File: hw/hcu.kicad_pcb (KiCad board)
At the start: 2 copper layers, 78 x 90 mm, 119 parts, among them J101 AMPSEAL_23_POS_VERT_BLACK_SEA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, J102 AMPSEAL_8_POS_VERT_BLACK_SEAL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, J201 ARM_JTAG_SWD_HEADER_10_PINSMD, U1001 VND5050AJTR-E, U1101 VND5050AJTR-E, U1201 VND5050AJTR-E, U1401 VN5E010AH, U201 MCP2551_SOIC8, U202 LPC1549JBD64, U301 VND5050AJTR-E, U401 VND5050AJTR-E, U501 VND5050AJTR-E, U601 VND5050AJTR-E, U701 VND5050AJTR-E, U801 VND5050AJTR-E, U901 VND5050AJTR-E, X201 XTAL_7A-12.000MAAJ-T

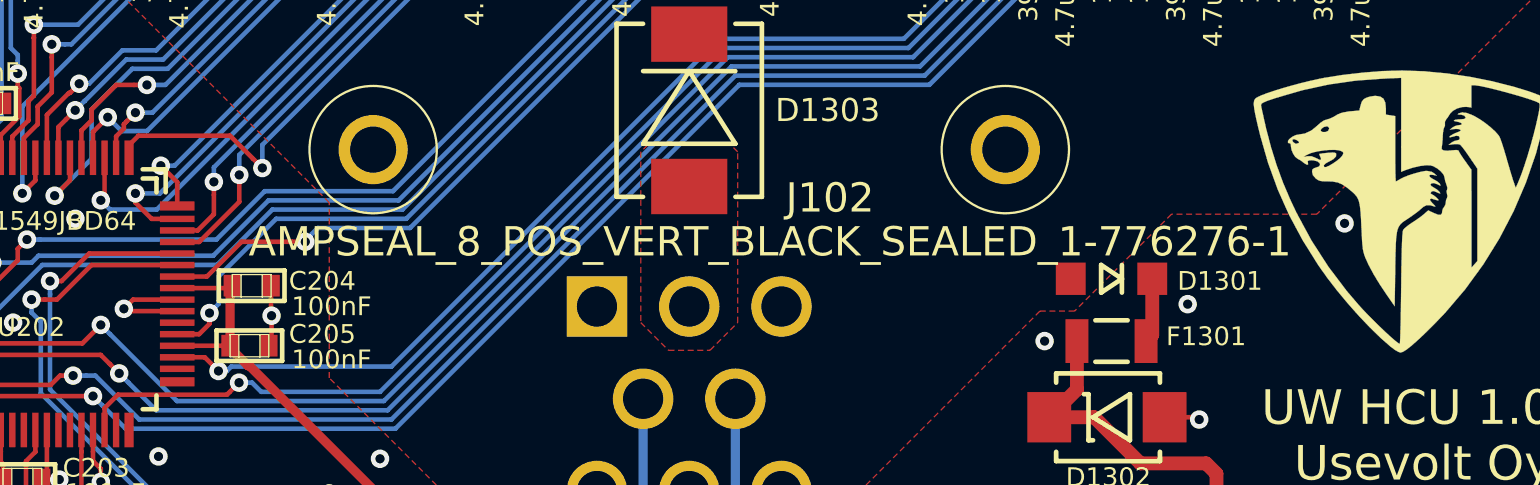
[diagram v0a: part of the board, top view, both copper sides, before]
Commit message: ampseal 8 pin changed to white one
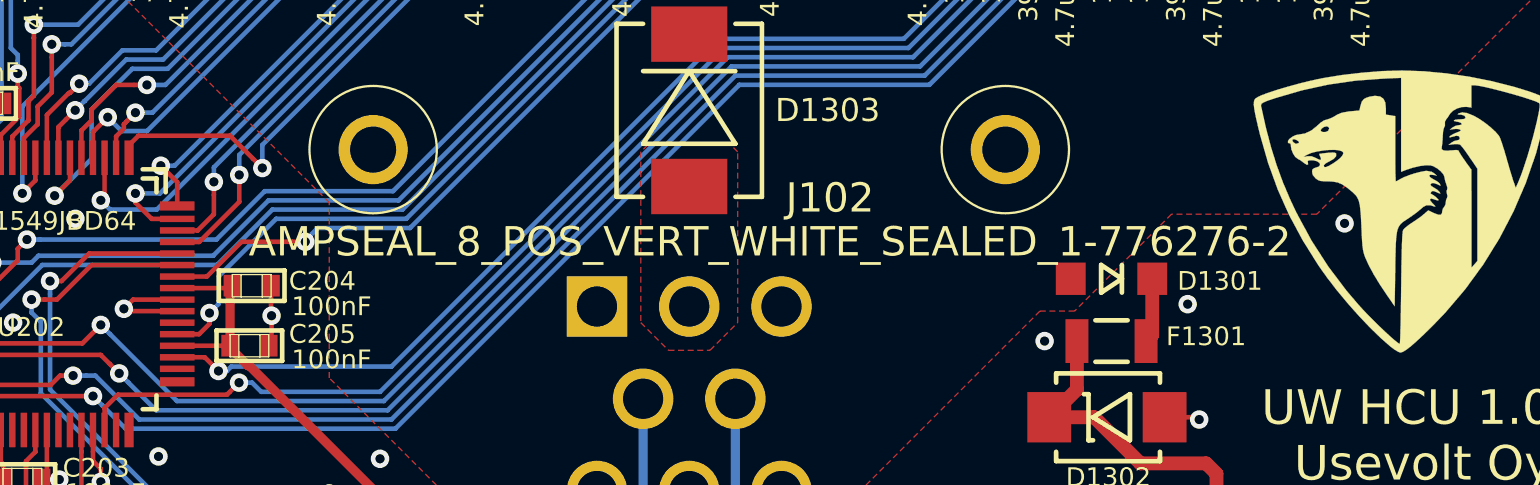
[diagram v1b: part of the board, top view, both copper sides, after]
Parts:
- J102: value AMPSEAL_8_POS_VERT_BLACK_SEALED_1-776276-1 -> AMPSEAL_8_POS_VERT_WHITE_SEALED_1-776276-2
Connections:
- J102 pad 6: VDD -> (no net)
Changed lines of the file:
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@@
     (add_net VDD)
   )
+  (module usevolt:SOT-23_3-PIN (layer F.Cu)
+    (at 160.354139 134.346 180)
+    (attr smd)
+    (fp_text reference VR1302 (at 0.354139 -2.754 180) (layer F.SilkS)
+      (effects (font (size 0.8128 0.8128) (thickness 0.0762)))
+    )
+    (fp_text value REG_MCP1700 (at 6 0 180) (layer F.SilkS) hide
+      (effects (font (size 0.8128 0.8128) (thickness 0.0762)))
+    )
+    (fp_line (start 1.4478 -0.54958) (end -1.4478 -0.54958) (layer F.SilkS) (width 0.19812))
+    (fp_line (start -1.4478 -0.54958) (end -1.4478 0.54958) (layer F.SilkS) (width 0.19812))
+    (fp_line (start 1.4478 -0.54958) (end 1.4478 0.54958) (layer F.SilkS) (width 0.19812))
+    (fp_line (start 1.4478 0.54958) (end -1.4478 0.54958) (layer F.SilkS) (width 0.19812))
+    (pad 1 smd rect (at -1 1.3 180) (size 0.7 1.35) (layers F.Cu F.Paste F.Mask)
+      (net 1 GND))
+    (pad 2 smd rect (at 1 1.3 180) (size 0.7 1.35) (layers F.Cu F.Paste F.Mask)
+      (net 2 +3V3))
+    (pad 3 smd rect (at 0 -1.3 180) (size 0.7 1.35) (layers F.Cu F.Paste F.Mask)
+      (net 3 +5V))
+    (model ${KISYS3DMOD}/SOT-23.wrl
+      (at (xyz 0 0 0))
+      (scale (xyz 0.3937 0.3937 0.3937))
+      (rotate (xyz 0 0 180))
+    )
+  )
   (module usevolt:uw_logo locked (layer F.Cu)
     (at 198.8 114.8)
@@
     )
   )
-  (module usevolt:SOT-23_3-PIN (layer F.Cu)
-    (at 160.354139 134.346 180)
-    (attr smd)
-    (fp_text reference VR1302 (at 0.354139 -2.754 180) (layer F.SilkS)
-      (effects (font (size 0.8128 0.8128) (thickness 0.0762)))
-    )
-    (fp_text value REG_MCP1700 (at 6 0 180) (layer F.SilkS) hide
-      (effects (font (size 0.8128 0.8128) (thickness 0.0762)))
-    )
-    (fp_line (start 1.4478 0.54958) (end -1.4478 0.54958) (layer F.SilkS) (width 0.19812))
-    (fp_line (start 1.4478 -0.54958) (end 1.4478 0.54958) (layer F.SilkS) (width 0.19812))
-    (fp_line (start -1.4478 -0.54958) (end -1.4478 0.54958) (layer F.SilkS) (width 0.19812))
-    (fp_line (start 1.4478 -0.54958) (end -1.4478 -0.54958) (layer F.SilkS) (width 0.19812))
-    (pad P$3 smd rect (at 0 -1.3 180) (size 0.7 1.35) (layers F.Cu F.Paste F.Mask)
-      (net 3 +5V))
-    (pad P$2 smd rect (at 1 1.3 180) (size 0.7 1.35) (layers F.Cu F.Paste F.Mask)
-      (net 2 +3V3))
-    (pad P$1 smd rect (at -1 1.3 180) (size 0.7 1.35) (layers F.Cu F.Paste F.Mask)
-      (net 1 GND))
-    (model ${KISYS3DMOD}/SOT-23.wrl
-      (at (xyz 0 0 0))
-      (scale (xyz 0.3937 0.3937 0.3937))
-      (rotate (xyz 0 0 180))
-    )
-  )
   (module usevolt:XTAL_7A-20.000MAJ (layer F.Cu)
     (at 133.8 130.4)
@@
       (effects (font (size 1.27 1.27) (thickness 0.1016)))
     )
-    (fp_text value AMPSEAL_8_POS_VERT_BLACK_SEALED_1-776276-1 (at 3.5 -6.8) (layer F.SilkS)
+    (fp_text value AMPSEAL_8_POS_VERT_WHITE_SEALED_1-776276-2 (at 3.5 -6.8) (layer F.SilkS)
       (effects (font (size 1.27 1.27) (thickness 0.1016)))
     )
@@
     (pad 5 thru_hole circle (at 1.99898 0) (size 2.62382 2.62382) (drill 1.74752) (layers *.Cu *.Mask)
       (net 9 /lpc1549/CANL))
-    (pad 6 thru_hole circle (at -3.99796 3.99796) (size 2.62382 2.62382) (drill 1.74752) (layers *.Cu *.Mask)
-      (net 4 VDD))
+    (pad 6 thru_hole circle (at -3.99796 3.99796) (size 2.62382 2.62382) (drill 1.74752) (layers *.Cu *.Mask))
     (pad 7 thru_hole circle (at 0 3.99796) (size 2.62382 2.62382) (drill 1.74752) (layers *.Cu *.Mask))
     (pad 8 thru_hole circle (at 3.99796 3.99796) (size 2.62382 2.62382) (drill 1.74752) (layers *.Cu *.Mask))

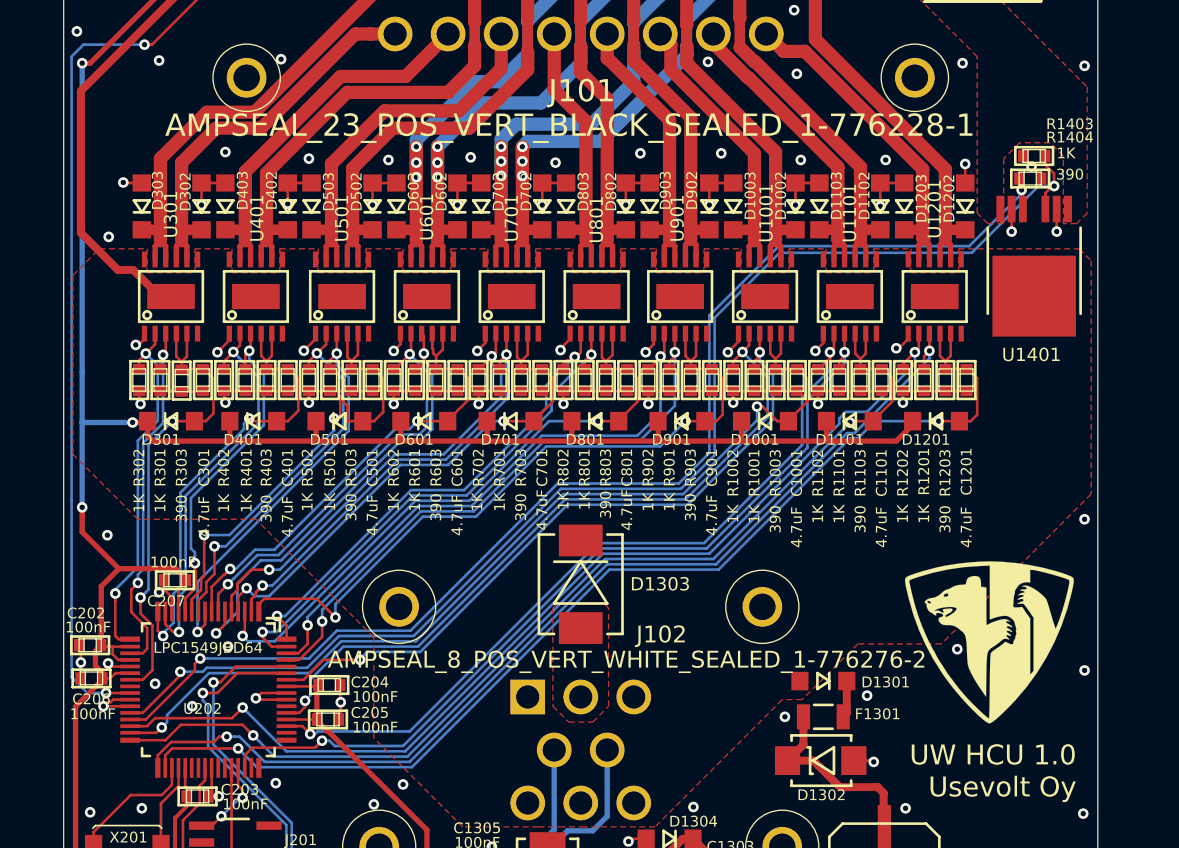
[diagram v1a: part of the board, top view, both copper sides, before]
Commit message: pull down resistor and flyback diode added to out11
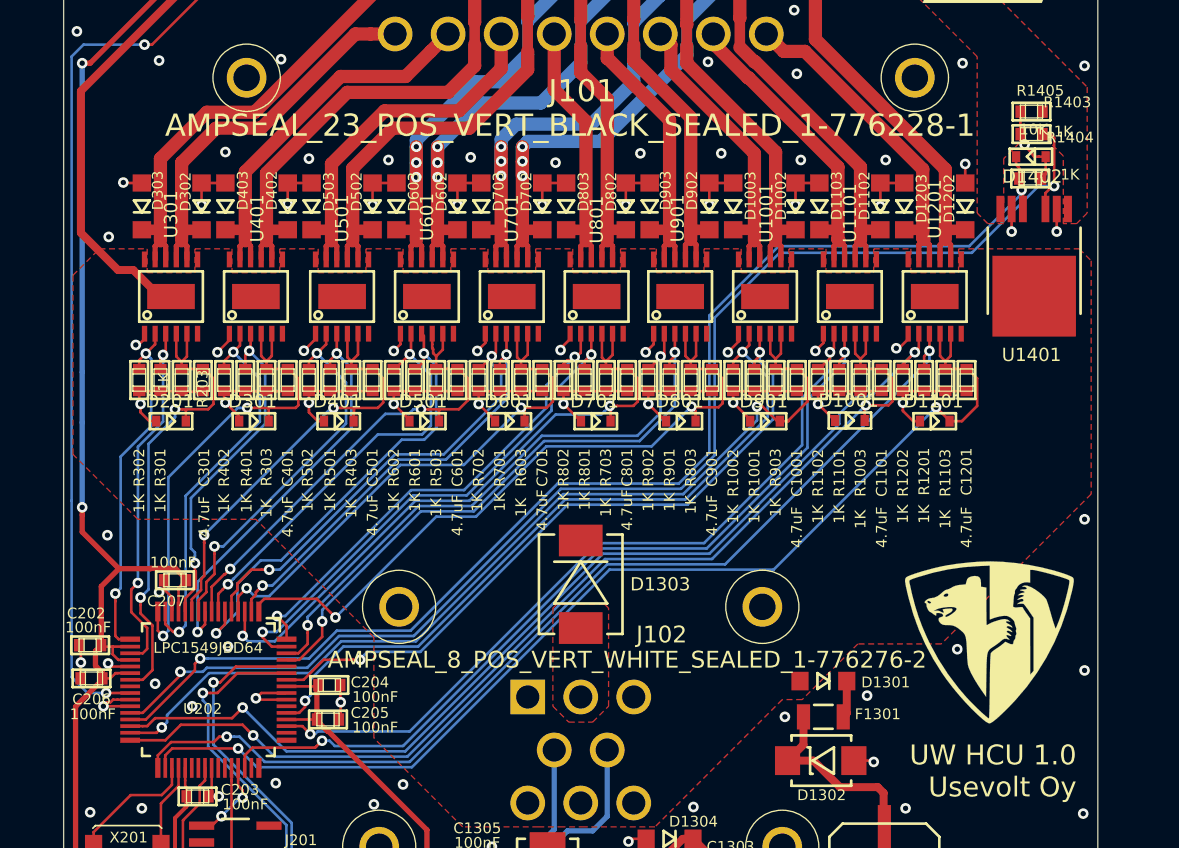
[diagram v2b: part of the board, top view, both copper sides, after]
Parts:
- removed D1201: DIODE_RS07J-GS18, usevolt:DO219AB
- removed R1203: 390, yageo:0603
- added D1402: ZENER_MM3Z3V6T1G, usevolt:SOD-323, F.Cu at (201.9, 78.2)
- added D201: ZENER_MM3Z3V6T1G, usevolt:SOD-323, F.Cu at (137.1, 98.2)
- added R1405: 10K, yageo:0603, F.Cu at (202.0, 74.8)
- added R203: 1K, yageo:0603, F.Cu at (137.9, 95.1)
- D1001, D1101, D301, D401, D501, D601, D701, D801, D901: value DIODE_RS07J-GS18 -> ZENER_MM3Z3V6T1G; footprint usevolt:DO219AB -> usevolt:SOD-323
- R1003, R1103, R1404, R303, R403, R503, R603, R703, R803, R903: value 390 -> 1K
- moved D601 6.45 mm to (162.7, 98.2)
- moved D801 6.45 mm to (175.6, 98.2)
- moved D401 6.45 mm to (149.8, 98.2)
- moved D701 6.44 mm to (169.1, 98.2)
- moved D1001 6.40 mm to (188.3, 98.2)
- moved R303 6.40 mm to (144.3, 95.1)
- moved R1003 6.40 mm to (189.1, 95.1)
- moved R1103 6.40 mm to (195.5, 95.1)
- moved R503 6.40 mm to (157.1, 95.1)
- moved R603 6.40 mm to (163.5, 95.1)
- moved R703 6.40 mm to (169.9, 95.1)
- moved R803 6.40 mm to (176.3, 95.1)
- moved D1101 6.40 mm to (194.7, 98.2)
- moved D501 6.40 mm to (156.2, 98.2)
- moved R403 6.40 mm to (150.7, 95.1)
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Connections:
- R1003 pad 1: /lpc1549/OUT8_SENSE -> /lpc1549/OUT9_SENSE
- R1103 pad 1: /lpc1549/OUT9_SENSE -> /lpc1549/OUT10_SENSE
- R303 pad 1: /lpc1549/OUT1_SENSE -> /lpc1549/OUT2_SENSE
- R403 pad 1: /lpc1549/OUT2_SENSE -> /lpc1549/OUT3_SENSE
- R503 pad 1: /lpc1549/OUT3_SENSE -> /lpc1549/OUT4_SENSE
- R603 pad 1: /lpc1549/OUT4_SENSE -> /lpc1549/OUT5_SENSE
- R703 pad 1: /lpc1549/OUT5_SENSE -> /lpc1549/OUT6_SENSE
- R803 pad 1: /lpc1549/OUT6_SENSE -> /lpc1549/OUT7_SENSE
- R903 pad 1: /lpc1549/OUT7_SENSE -> /lpc1549/OUT8_SENSE
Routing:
- net +3V3: track 266.9 -> 190.1 mm, vias 3 -> 2
- net GND: track 160.2 -> 183.8 mm
- net /lpc1549/OUT3_SENSE: track 37.6 -> 34.4 mm
- net /Sheet5ABCCFA6/IN1: track 96.9 -> 99.1 mm
- net /lpc1549/OUT11_SENSE: track 92.7 -> 94.5 mm
- net /lpc1549/OUT2_SENSE: track 35.4 -> 37.0 mm
- net /lpc1549/OUT9_SENSE: track 79.4 -> 80.6 mm
- net /lpc1549/OUT6_SENSE: track 48.9 -> 50.1 mm
- net /lpc1549/OUT5_SENSE: track 41.0 -> 42.1 mm
- net /lpc1549/OUT1_SENSE: track 36.0 -> 36.9 mm
- net /lpc1549/OUT4_SENSE: track 36.1 -> 37.0 mm

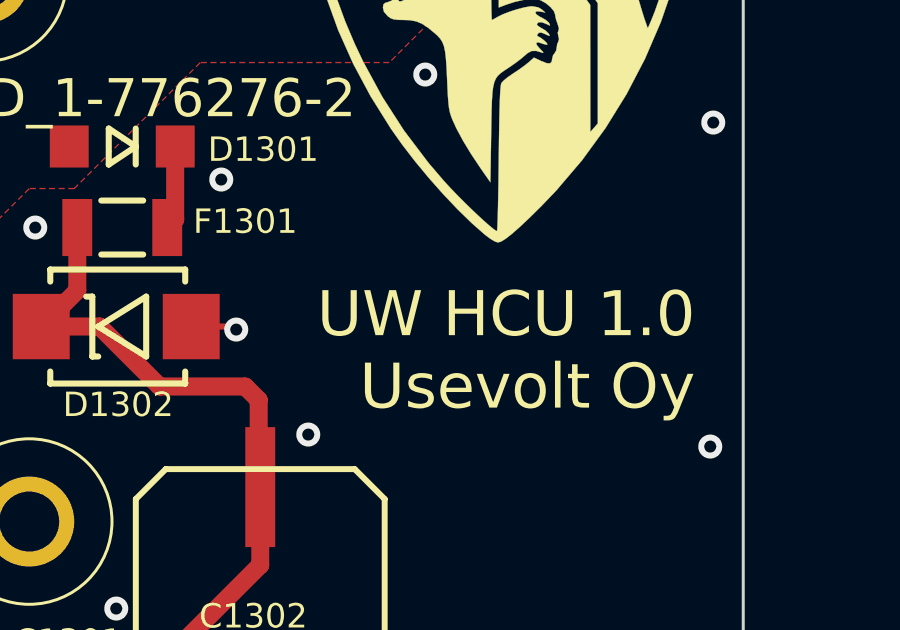
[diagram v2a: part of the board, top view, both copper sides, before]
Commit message: sense protection diodes changed to zeners
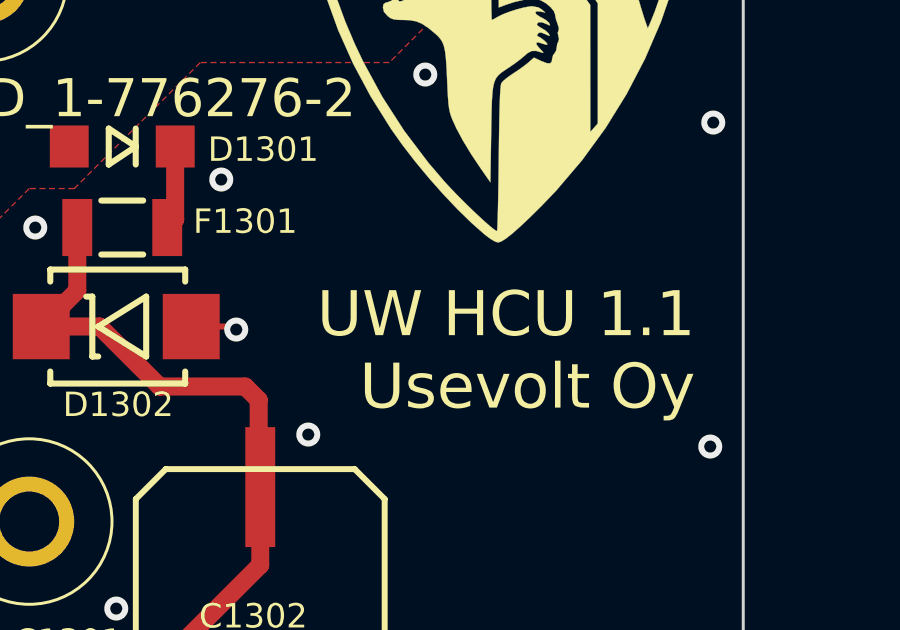
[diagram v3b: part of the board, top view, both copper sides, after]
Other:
- board text added: "UW HCU 1.1 Usevolt Oy"
- board text removed: "UW HCU 1.0 Usevolt Oy"
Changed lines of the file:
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@@
     (arrow2b (pts (xy 209.747154 49.003578) (xy 210.333575 50.130082)))
   )
-  (gr_text "UW HCU 1.0\nUsevolt Oy" (at 205.4 124.6) (layer F.SilkS)
+  (gr_text "UW HCU 1.1\nUsevolt Oy" (at 205.4 124.6) (layer F.SilkS)
     (effects (font (size 1.5 1.5) (thickness 0.3)) (justify right))
   )

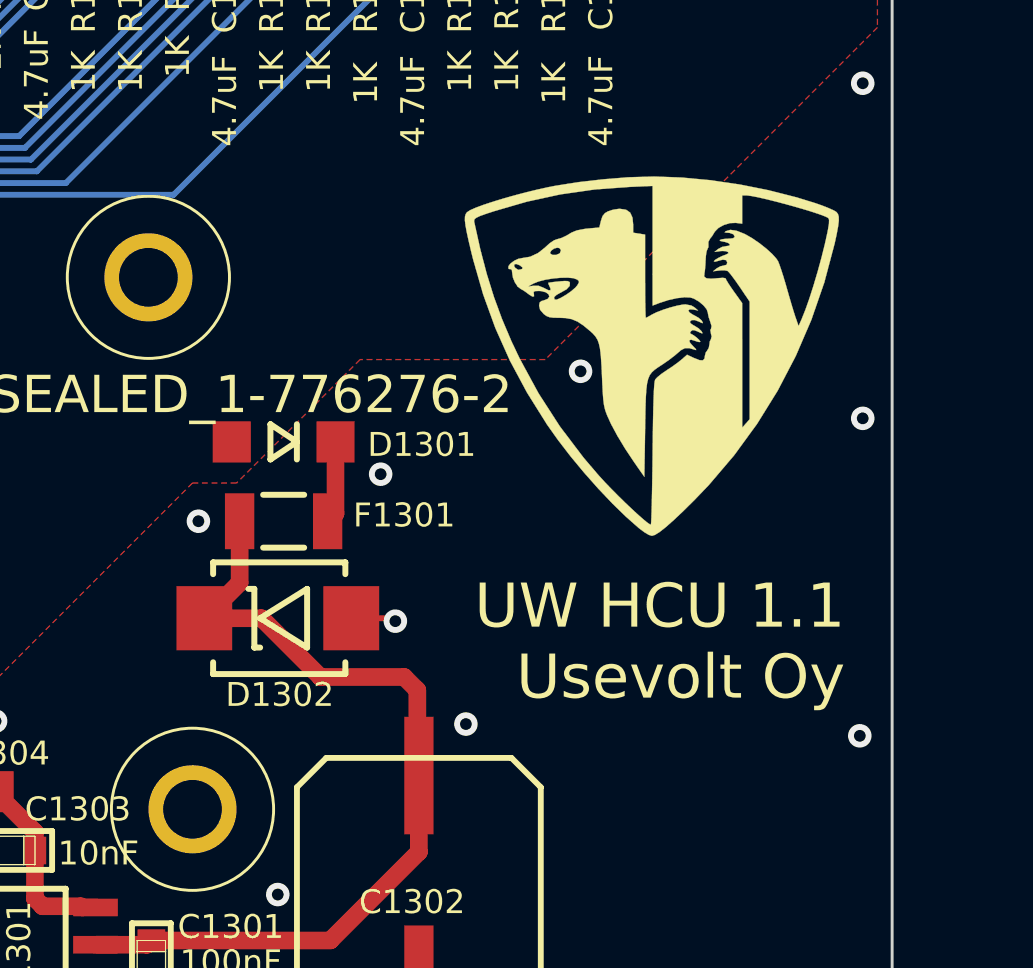
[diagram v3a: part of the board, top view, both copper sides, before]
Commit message: enclosure ready for cnc'd, added heatsink to mosfets
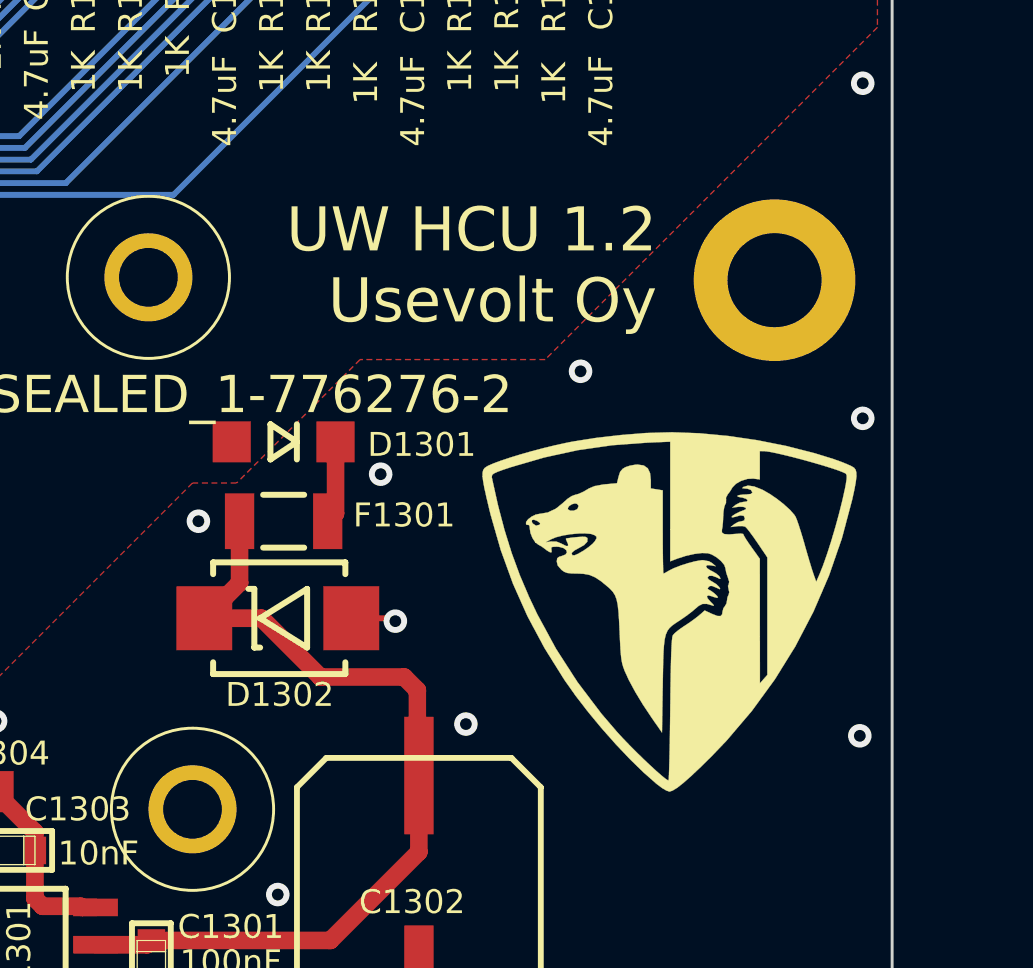
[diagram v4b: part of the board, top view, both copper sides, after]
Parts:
- added REF**: MOUNTING_HOLE, usevolt:MOUNTING_HOLE, F.Cu at (203.0, 112.3)
- moved G*** 8.72 mm to (199.4, 123.5)
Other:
- board text added: "UW HCU 1.2 Usevolt Oy"
- board text removed: "UW HCU 1.1 Usevolt Oy"
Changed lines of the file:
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@@
     (tracks 1502)
     (zones 0)
-    (modules 121)
+    (modules 122)
     (nets 74)
   )
@@
   )
   (module usevolt:uw_logo locked (layer F.Cu)
-    (at 198.8 114.8)
+    (at 199.4 123.5)
     (fp_text reference G*** (at 0 0) (layer F.SilkS) hide
       (effects (font (size 1.524 1.524) (thickness 0.3)))
@@
     )
   )
+  (module usevolt:MOUNTING_HOLE (layer F.Cu)
+    (at 203 112.3)
+    (fp_text reference REF** (at 0 -2.9972) (layer F.SilkS) hide
+      (effects (font (size 1 1) (thickness 0.15)))
+    )
+    (fp_text value MOUNTING_HOLE (at 0 -2.9972) (layer F.Fab) hide
+      (effects (font (size 1 1) (thickness 0.15)))
+    )
+    (pad "" np_thru_hole circle (at 0 0) (size 5.5 5.5) (drill 3.2) (layers *.Cu *.Mask))
+  )
   (gr_arc (start 131 137.000232) (end 131 139.000232) (angle 90) (layer Edge.Cuts) (width 0.1))
   (gr_arc (start 205 137) (end 207 137) (angle 90) (layer Edge.Cuts) (width 0.1))
@@
     (arrow2b (pts (xy 209.747154 49.003578) (xy 210.333575 50.130082)))
   )
-  (gr_text "UW HCU 1.1\nUsevolt Oy" (at 205.4 124.6) (layer F.SilkS)
+  (gr_text "UW HCU 1.2\nUsevolt Oy" (at 199 111.8) (layer F.SilkS)
     (effects (font (size 1.5 1.5) (thickness 0.3)) (justify right))
   )
